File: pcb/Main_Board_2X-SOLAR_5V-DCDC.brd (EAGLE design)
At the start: 82.6 x 34.3 mm, 72 parts, among them CN5 USBA_FEMALE, IC1 MCP73871, IC2 MCP73871, T2 MMUN2133LT1G, U3 TPS61090RSAR, X1 Solar input, X2 5V output

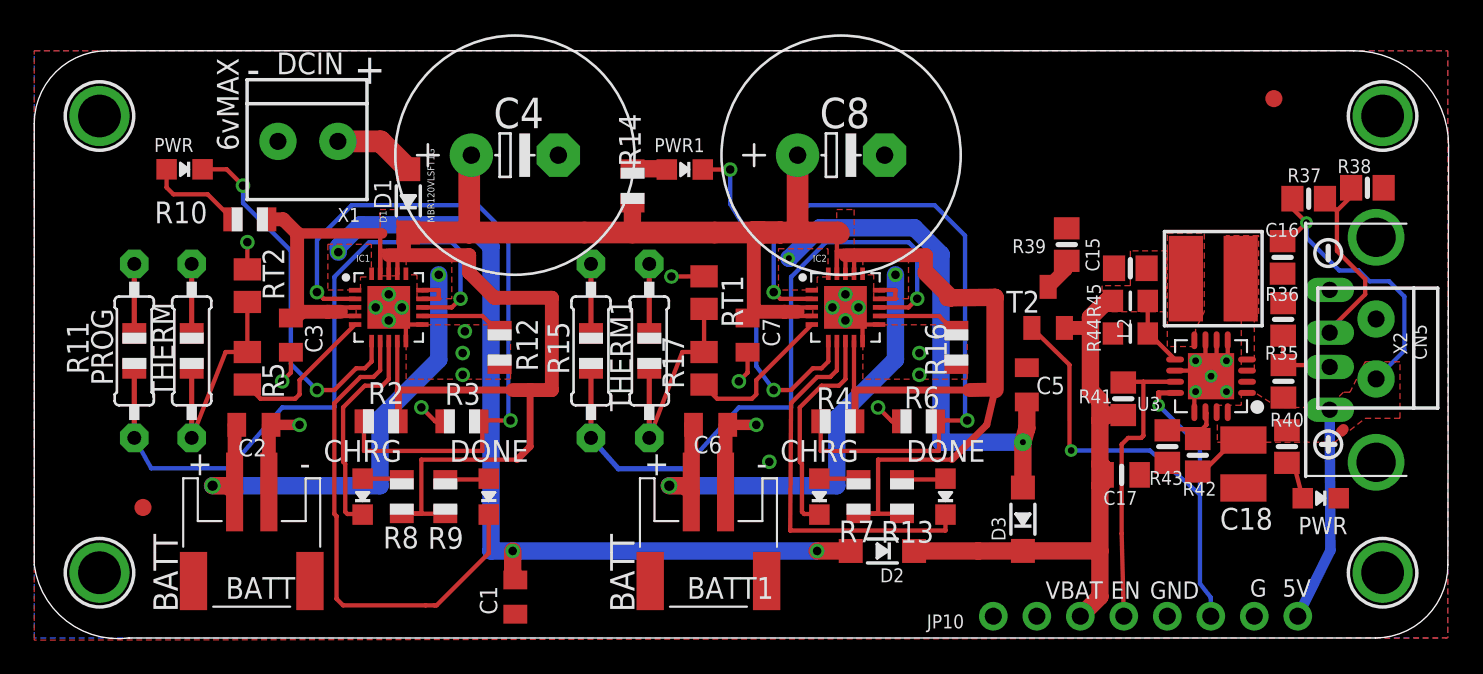
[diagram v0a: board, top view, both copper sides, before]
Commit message: Added LT4015 footprints to eagle and began routing
LTC4015 chip footprints and schematic uploaded to eagle library. Routing started for new board. Removed all routings so only airwires exist at this point.
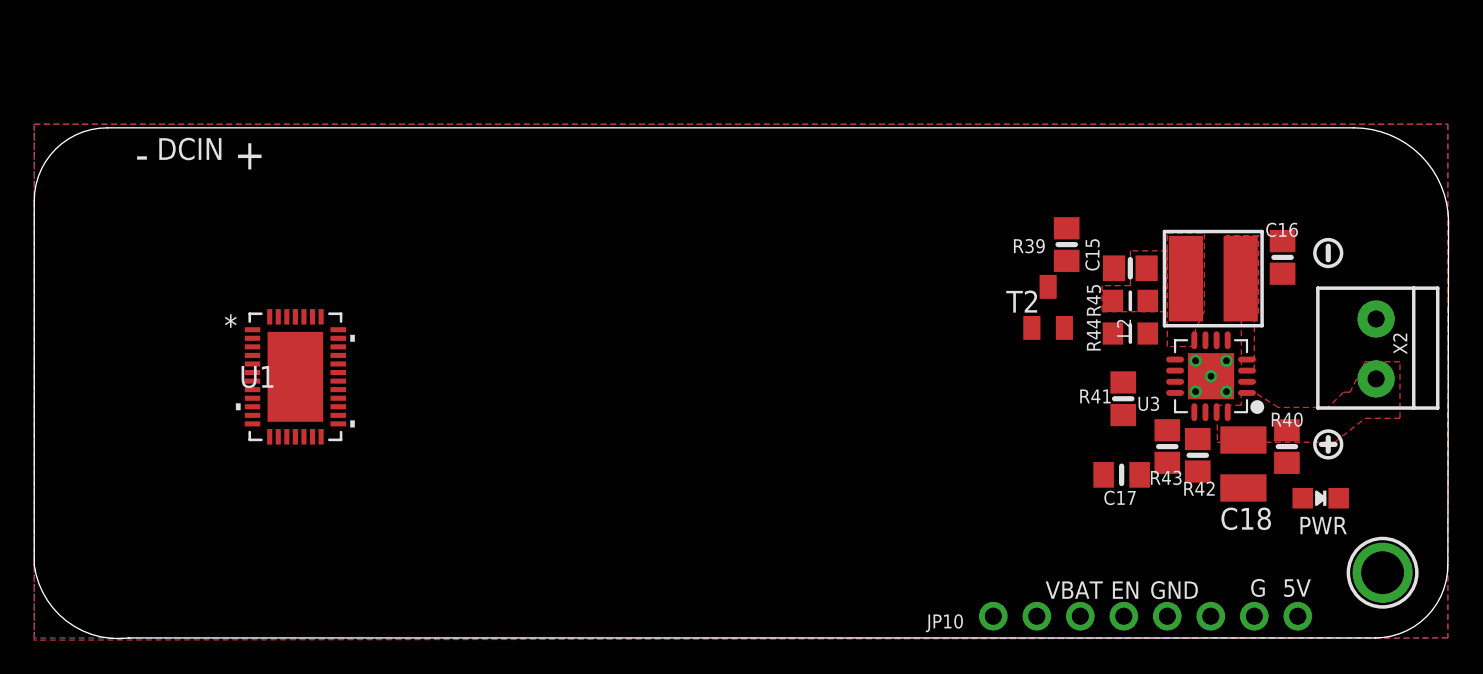
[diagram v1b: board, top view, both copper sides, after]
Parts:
- removed BATT, BATT1: 3.7V Li-ion, adafruit:JST-PH-2-SMT-RA
- removed C1, C2, C3, C5, C6, C7: 10uF, adafruit:C0805K
- removed C4, C8: 4700uF/10V, adafruit:E5-13
- removed CHRG/LBO, CHRG/LBO1: ORANGE, microbuilder:CHIPLED_0805_NOOUTLINE
- removed CN5: USBA_FEMALE, microbuilder:USB_HOST-PTH
- removed D1, D2, D3: MBR120VLSFT1G, microbuilder:SOD-123
- removed DONE, DONE1: GREEN, microbuilder:CHIPLED_0805_NOOUTLINE
- removed IC1, IC2: MCP73871, adafruit:QFN20_4MM
- removed PWR, PWR1: RED, microbuilder:CHIPLED_0805_NOOUTLINE
- removed R10, R13, R14, R7, R8, R9: 1K, adafruit:R0805
- removed R11, R15: 1K, adafruit:0805-THM
- removed R12, R16, R3, R6: 100K, adafruit:R0805
- removed R17, R5: 1K, adafruit:M0805
- removed R2, R4: 270K, adafruit:R0805
- removed R35: 43K, microbuilder:0805-NO
- removed R36: 49.9K, microbuilder:0805-NO
- removed R37: 75K 1%, microbuilder:0805-NO
- removed R38: 49.9K 1%, microbuilder:0805-NO
- removed RT1, RT2: 150K, adafruit:M0805
- removed THERM, THERM1: 10K, adafruit:0805-THM
- removed U$1, U$4, U$6: MOUNTINGHOLE2.5, microbuilder:MOUNTINGHOLE_2.5_PLATED
- removed U$3, U$8: FIDUCIAL, adafruit:FIDUCIAL_1MM
- removed X1: Solar input, microbuilder:TERMBLOCK_1X2-3.5MM
- added U1: LTC4015EUHFPBFQFN-38_UHF-M, LTC4015_LTC4015EUHF&hash_PBF:QFN-38_UHF-M
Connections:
- removed net BATT: BATT.1, C2.1, IC1.P$14, IC1.P$15, IC1.P$16
- removed net BATT1: BATT1.1, C6.1, IC2.P$14, IC2.P$15, IC2.P$16
- removed net D+1: CN5.D+, R37.1, R38.1
- removed net D-1: CN5.D-, R35.1, R36.1
- removed net N$12: CHRG/LBO.A, R8.1
- removed net N$13: DONE.A, R9.1
- removed net N$14: PWR.A, R10.1
- removed net N$19: CHRG/LBO1.A, R7.1
- removed net N$20: DONE1.A, R13.1
- removed net N$21: PWR1.A, R14.1
- removed net N$24: IC2.P$5, R17.1
- removed net N$25: R17.2, RT1.2, THERM1.2
- removed net N$5: IC1.P$5, R5.1
- removed net N$8: R5.2, RT2.2, THERM.2
- removed net PG: IC1.P$6, PWR.C
- removed net PG_1: IC2.P$6, PWR1.C
- removed net PROG1: IC1.P$13, R11.2
- removed net PROG1_1: IC2.P$13, R15.2
- removed net PROG3: IC1.P$12, R12.2
- removed net PROG3_1: IC2.P$12, R16.2
- removed net PV_IN: D1.A, X1.2
- removed net STAT1: CHRG/LBO.C, IC1.P$8
- removed net STAT1_1: CHRG/LBO1.C, IC2.P$8
- removed net STAT2: DONE.C, IC1.P$7
- removed net STAT2_1: DONE1.C, IC2.P$7
- removed net VCC: C3.1, C4.+, C7.1, C8.+, D1.C, IC1.P$17, IC1.P$18, IC1.P$19, IC1.P$3, IC1.P$4, IC1.P$9, IC2.P$17, IC2.P$18, IC2.P$19, IC2.P$3, IC2.P$4, IC2.P$9, R10.2, R13.2, R14.2, R2.2, R4.2, R7.2, R8.2, R9.2
- removed net VOUT: C1.1, D2.A, IC1.P$1, IC1.P$20
- removed net VOUT1: C5.1, D3.A, IC2.P$1, IC2.P$20
- removed net VPCC: IC1.P$2, R2.1, R3.1
- removed net VPCC1: IC2.P$2, R4.1, R6.1
- new net DVCC: U1.3
- new net GND_2: U1.14
- new net SGND: U1.7
- net 5.0V: no longer CN5.VBUS, R35.2, R37.2
- net GND: now also U1.39; no longer BATT.2, BATT1.2, C1.2, C2.2, C3.2, C4.-, C5.2, C6.2, C7.2, C8.-, CN5.GND, IC1.P$10, IC1.P$11, IC1.P$21, IC2.P$10, IC2.P$11, IC2.P$21, R11.1, R12.1, R15.1, R16.1, R3.2, R36.2, R38.2, R6.2, RT1.1, RT2.1, THERM.1, THERM1.1, X1.1
- net VBAT: no longer D2.C, D3.C
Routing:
- net VCC: track 181.1 -> 0.00 mm
- net VOUT: track 50.8 -> 0.00 mm, vias 3 -> 0
- net VPCC1: track 41.8 -> 0.00 mm, vias 2 -> 0
- net VPCC: track 41.8 -> 0.00 mm, vias 2 -> 0
- net GND: track 37.9 -> 0.00 mm, vias 22 -> 0
- net PROG1: track 35.6 -> 0.00 mm, vias 1 -> 0
- net PROG1_1: track 35.4 -> 0.00 mm, vias 1 -> 0
- net VBAT: track 35.3 -> 0.00 mm
- net 5.0V: track 34.5 -> 0.00 mm, vias 1 -> 0
- net T2-BASE_LBO: track 32.1 -> 0.00 mm, vias 2 -> 0
- net BATT1: track 31.7 -> 0.00 mm, vias 2 -> 0
- net BATT: track 31.7 -> 0.00 mm, vias 2 -> 0
- net VOUT1: track 31.4 -> 0.00 mm, vias 2 -> 0
- net STAT2: track 29.2 -> 0.00 mm
- net STAT2_1: track 22.6 -> 0.00 mm
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- removed copper zone on layer 1, net BATT
- removed copper zone on layer 1, net BATT1
- removed copper zone on layer 1, net VCC
- removed copper zone on layer 1, net VOUT
- removed copper zone on layer 1, net VOUT1
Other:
- board size 82.6 x 34.3 mm -> 82.6 x 29.8 mm
- board text added: "LiFePO4 Batteries Only! 3.2 V / 3.6 V"
- board text removed: "(3.7/4.2V Batteries)"
- board text removed: ".GND."
- board text removed: "1000/PROG"
- board text removed: "5.0-6.5V"
- board text removed: "6vMAX"
- board text removed: "BATT"
- board text removed: "CHRG"
- board text removed: "CHRG RATE"
- board text removed: "D1"
- board text removed: "DC INPUT"
- board text removed: "DONE"
- board text removed: "MCP73871 USB/Solar"
- board text removed: "PROG"

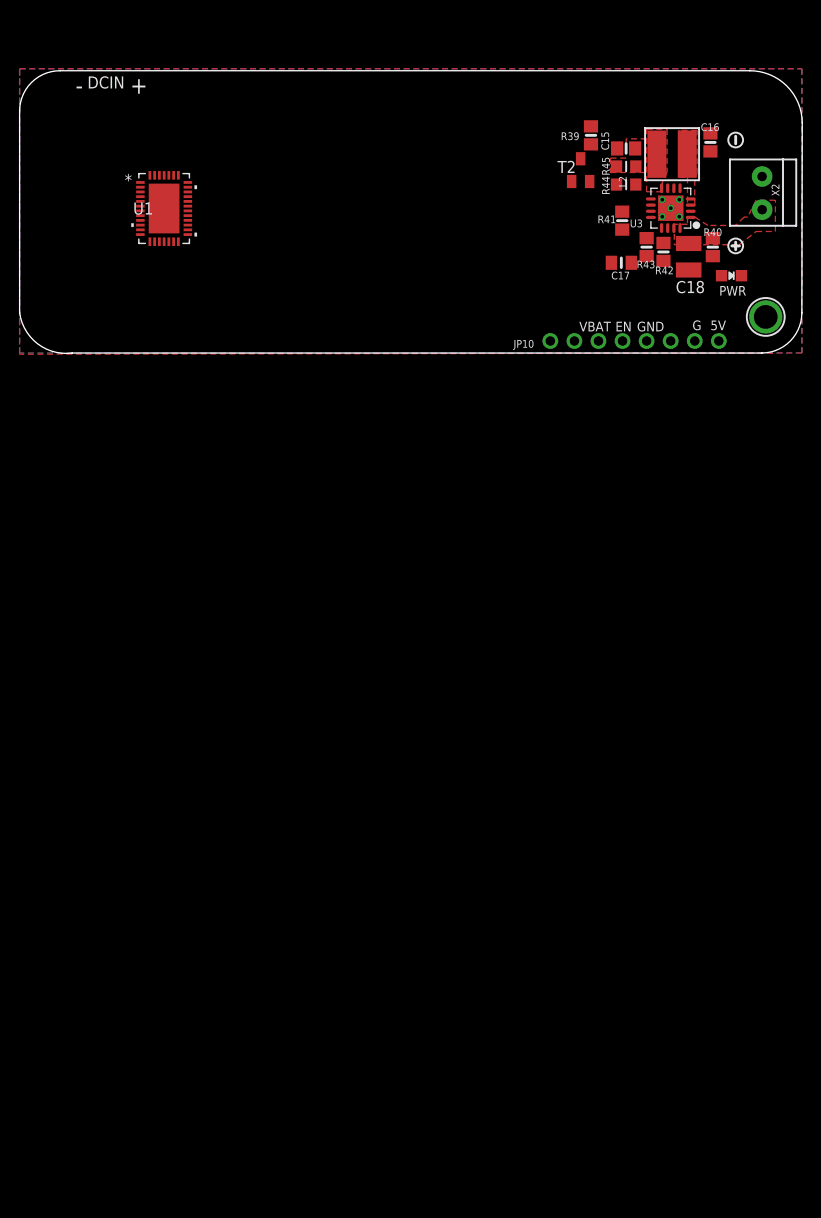
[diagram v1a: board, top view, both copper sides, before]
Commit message: Footprint added and began LTC4015 layout
Created LTC4015 footprint in library and schematic. Updated BOM for original board with prices for each part and consolidated parts
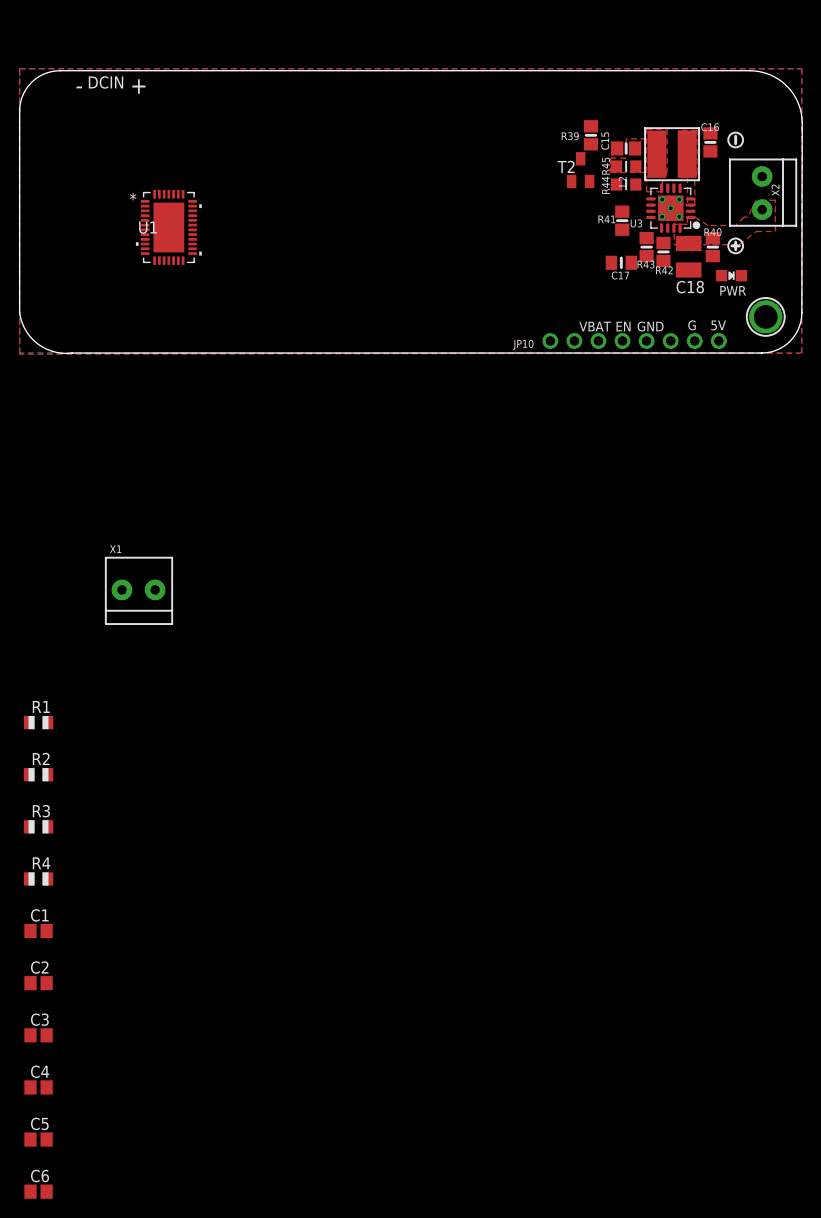
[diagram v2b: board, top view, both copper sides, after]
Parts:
- added C1, C2, C3, C4, C5, C6: (no value), adafruit:C0805
- added R1, R2, R3, R4: (no value), adafruit:R0805
- added X1: 6V_PV, microbuilder:TERMBLOCK_1X2-3.5MM
- moved U1 2.06 mm to (15.8, 13.2)
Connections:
- net GND: now also U1.1, U1.2, X1.1
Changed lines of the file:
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@@
 <layer number="20" name="Dimension" color="15" fill="1" visible="yes" active="yes"/>
 <layer number="21" name="tPlace" color="7" fill="1" visible="yes" active="yes"/>
-<layer number="22" name="bPlace" color="7" fill="1" visible="yes" active="yes"/>
+<layer number="22" name="bPlace" color="7" fill="1" visible="no" active="yes"/>
 <layer number="23" name="tOrigins" color="15" fill="1" visible="yes" active="yes"/>
-<layer number="24" name="bOrigins" color="15" fill="1" visible="yes" active="yes"/>
-<layer number="25" name="tNames" color="7" fill="1" visible="yes" active="yes"/>
-<layer number="26" name="bNames" color="7" fill="1" visible="yes" active="yes"/>
-<layer number="27" name="tValues" color="7" fill="1" visible="yes" active="yes"/>
-<layer number="28" name="bValues" color="7" fill="1" visible="yes" active="yes"/>
+<layer number="24" name="bOrigins" color="15" fill="1" visible="no" active="yes"/>
+<layer number="25" name="tNames" color="7" fill="1" visible="no" active="yes"/>
+<layer number="26" name="bNames" color="7" fill="1" visible="no" active="yes"/>
+<layer number="27" name="tValues" color="7" fill="1" visible="no" active="yes"/>
+<layer number="28" name="bValues" color="7" fill="1" visible="no" active="yes"/>
 <layer number="29" name="tStop" color="7" fill="3" visible="no" active="yes"/>
 <layer number="30" name="bStop" color="7" fill="6" visible="no" active="yes"/>
@@
 <layer number="56" name="wert" color="7" fill="1" visible="no" active="yes"/>
 <layer number="57" name="tCAD" color="7" fill="1" visible="no" active="no"/>
+<layer number="59" name="tCarbon" color="7" fill="1" visible="no" active="no"/>
+<layer number="60" name="bCarbon" color="7" fill="1" visible="no" active="no"/>
 <layer number="90" name="Modules" color="5" fill="1" visible="no" active="no"/>
 <layer number="91" name="Nets" color="2" fill="1" visible="no" active="no"/>
@@
 <layer number="127" name="_tValues" color="7" fill="1" visible="no" active="yes"/>
 <layer number="128" name="_bValues" color="7" fill="1" visible="no" active="yes"/>
+<layer number="129" name="Mask" color="7" fill="1" visible="yes" active="yes"/>
 <layer number="131" name="tAdjust" color="7" fill="1" visible="no" active="yes"/>
 <layer number="132" name="bAdjust" color="7" fill="1" visible="no" active="yes"/>
@@
 <layer number="223" name="223bmp" color="24" fill="1" visible="no" active="no"/>
 <layer number="224" name="224bmp" color="25" fill="1" visible="no" active="no"/>
+<layer number="225" name="225bmp" color="7" fill="1" visible="yes" active="yes"/>
+<layer number="226" name="226bmp" color="7" fill="1" visible="yes" active="yes"/>
+<layer number="227" name="227bmp" color="7" fill="1" visible="yes" active="yes"/>
+<layer number="228" name="228bmp" color="7" fill="1" visible="yes" active="yes"/>
+<layer number="229" name="229bmp" color="7" fill="1" visible="yes" active="yes"/>
+<layer number="230" name="230bmp" color="7" fill="1" visible="yes" active="yes"/>
 <layer number="231" name="Eagle3D_PG1" color="7" fill="1" visible="no" active="no"/>
 <layer number="232" name="Eagle3D_PG2" color="7" fill="1" visible="no" active="no"/>
@@
 <layer number="251" name="SMDround" color="7" fill="1" visible="no" active="no"/>
 <layer number="254" name="cooling" color="7" fill="1" visible="no" active="yes"/>
+<layer number="255" name="routoute" color="7" fill="1" visible="yes" active="yes"/>
 </layers>
 <board>
@@
 <text x="73.66" y="28.6766" size="1.27" layer="22" ratio="12" rot="MR0">USB: 1A Charge Rate</text>
 <text x="72.898" y="2.413" size="1.016" layer="21" ratio="12">5V</text>
-<text x="70.993" y="2.413" size="1.016" layer="21" ratio="12">G</text>
+<text x="70.493" y="2.413" size="1.016" layer="21" ratio="12">G</text>
 <text x="65.151" y="2.286" size="1.016" layer="21" ratio="12">GND</text>
 <text x="11.899" y="26.742" size="1.27" layer="22" font="vector" rot="MR180">+6V</text>
@@
 <element name="U3" library="microbuilder" package="PVQFN-16" value="TPS61090RSAR" x="68.721" y="15.286" smashed="yes" rot="R180">
 <attribute name="NAME" x="64.397" y="13.268" size="0.8128" layer="25" ratio="18"/>
-<attribute name="VALUE" x="68.342" y="4.17" size="1.016" layer="27" font="vector" ratio="10" rot="R270"/>
+<attribute name="VALUE" x="63.83" y="15.342" size="1.016" layer="27" font="vector" ratio="10"/>
 </element>
 <element name="L2" library="microbuilder" package="INDUCTOR_5X5MM_TDK_VLC5045" value="6.8uH" x="68.852" y="20.984" smashed="yes">
@@
 <element name="JP10" library="microbuilder" package="1X08_ROUND" value="5V step up jumpers" x="64.897" y="1.27" smashed="yes">
 <attribute name="NAME" x="52.1208" y="0.5588" size="0.8128" layer="25" ratio="18"/>
-<attribute name="VALUE" x="54.737" y="-1.905" size="0.4064" layer="27" ratio="10"/>
-</element>
-<element name="U1" library="LTC4015_LTC4015EUHF&amp;hash_PBF" package="QFN-38_UHF-M" value="LTC4015EUHFPBFQFN-38_UHF-M" x="15.25" y="15.25">
-<attribute name="MANUFACTURER_PART_NUMBER" value="ltc4015euhf#pbf" x="15.25" y="15.25" size="1.778" layer="27" display="off"/>
-<attribute name="VENDOR" value="Linear Technology" x="15.25" y="15.25" size="1.778" layer="27" display="off"/>
-</element>
+<attribute name="VALUE" x="61.737" y="-0.905" size="0.4064" layer="27" ratio="10"/>
+</element>
+<element name="U1" library="LTC4015_LTC4015EUHF&amp;hash_PBF" package="QFN-38_UHF-M" value="LTC4015EUHFPBFQFN-38_UHF-M" x="15.75" y="13.25">
+<attribute name="MANUFACTURER_PART_NUMBER" value="ltc4015euhf#pbf" x="15.75" y="13.25" size="1.778" layer="27" display="off"/>
+<attribute name="VENDOR" value="Linear Technology" x="15.75" y="13.25" size="1.778" layer="27" display="off"/>
+</element>
+<element name="X1" library="microbuilder" package="TERMBLOCK_1X2-3.5MM" value="6V_PV" x="12.5" y="-25"/>
+<element name="R1" library="adafruit" library_urn="urn:adsk.eagle:library:420" package="R0805" value="" x="2" y="-39"/>
+<element name="R2" library="adafruit" library_urn="urn:adsk.eagle:library:420" package="R0805" value="" x="2" y="-44.5"/>
+<element name="R3" library="adafruit" library_urn="urn:adsk.eagle:library:420" package="R0805" value="" x="2" y="-50"/>
+<element name="R4" library="adafruit" library_urn="urn:adsk.eagle:library:420" package="R0805" value="" x="2" y="-55.5"/>
+<element name="C1" library="adafruit" library_urn="urn:adsk.eagle:library:420" package="C0805" value="" x="2" y="-61"/>
+<element name="C2" library="adafruit" library_urn="urn:adsk.eagle:library:420" package="C0805" value="" x="2" y="-66.5"/>
+<element name="C3" library="adafruit" library_urn="urn:adsk.eagle:library:420" package="C0805" value="" x="2" y="-72"/>
+<element name="C4" library="adafruit" library_urn="urn:adsk.eagle:library:420" package="C0805" value="" x="2" y="-77.5"/>
+<element name="C5" library="adafruit" library_urn="urn:adsk.eagle:library:420" package="C0805" value="" x="2" y="-83"/>
+<element name="C6" library="adafruit" library_urn="urn:adsk.eagle:library:420" package="C0805" value="" x="2" y="-88.5"/>
 </elements>
 <signals>
@@
 <contactref element="R39" pad="1"/>
 <contactref element="U1" pad="39"/>
+<contactref element="X1" pad="1"/>
+<contactref element="U1" pad="2"/>
+<contactref element="U1" pad="1"/>
 <wire x1="72.898" y1="21.275" x2="78.359" y2="18.6275" width="0" layer="19" extent="1-1"/>
 <wire x1="69.696" y1="17.386" x2="72.898" y2="21.275" width="0" layer="19" extent="1-1"/>
@@
 <wire x1="71.247" y1="1.27" x2="70.612" y2="8.76" width="0" layer="19" extent="1-1"/>
 <wire x1="66.167" y1="1.27" x2="71.247" y2="1.27" width="0" layer="19" extent="1-1"/>
-<wire x1="15.25" y1="15.25" x2="60.293" y2="23.923" width="0" layer="19" extent="1-1"/>
+<wire x1="15.75" y1="13.25" x2="60.293" y2="23.923" width="0" layer="19" extent="1-1"/>
+<wire x1="13.2468" y1="15.5" x2="15.75" y2="13.25" width="0" layer="19" extent="1-1"/>
+<wire x1="13.2468" y1="16" x2="13.2468" y2="15.5" width="0" layer="19" extent="1-1"/>
+<wire x1="14.3" y1="-25" x2="15.75" y2="13.25" width="0" layer="19" extent="1-1"/>
 </signal>
 <signal name="SW">
@@
 which will not be processed correctly with this version.
 </note>
+<note version="8.2" severity="warning">
+Since Version 8.2, Eagle supports online libraries. The ids
+of those online libraries will not be understood (or retained)
+with this version.
+</note>
 </compatibility>
